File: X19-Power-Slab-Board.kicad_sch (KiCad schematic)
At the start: 41 parts, among them J1 Conn_01x04_Pin, J10 Conn_01x02, J11 Conn_01x02, J12 Conn_01x02, J13 Conn_01x02, J14 Conn_01x02, J15 Conn_01x02, J16 Conn_01x02, J2 Conn_01x02_Pin, J3 Conn_01x04_Pin, J4 796636-6, J5 Conn_01x05, J6 Conn_01x05, J8 Conn_01x02, J9 Conn_01x03_Pin, Q1 TSM340N06CP_ROG, U1 TCAN1044AVDRQ1, U3 TMP1075NDRLR

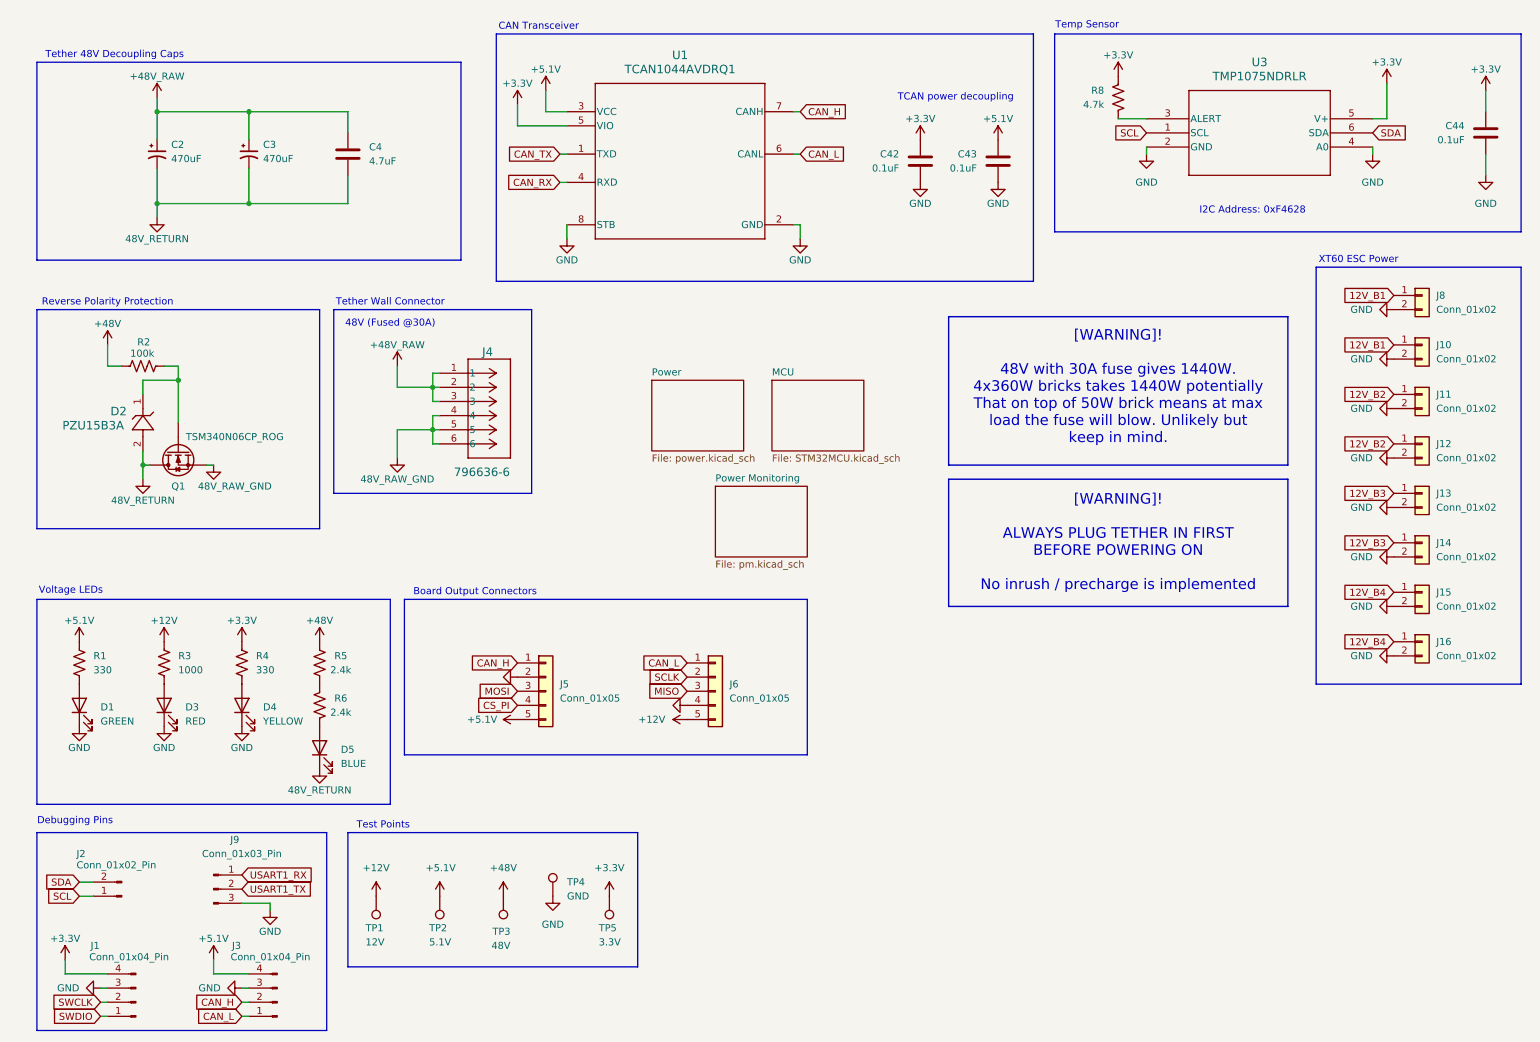
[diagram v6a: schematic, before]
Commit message: Prettified, more power changes and MCU pin changes and removing redundancies
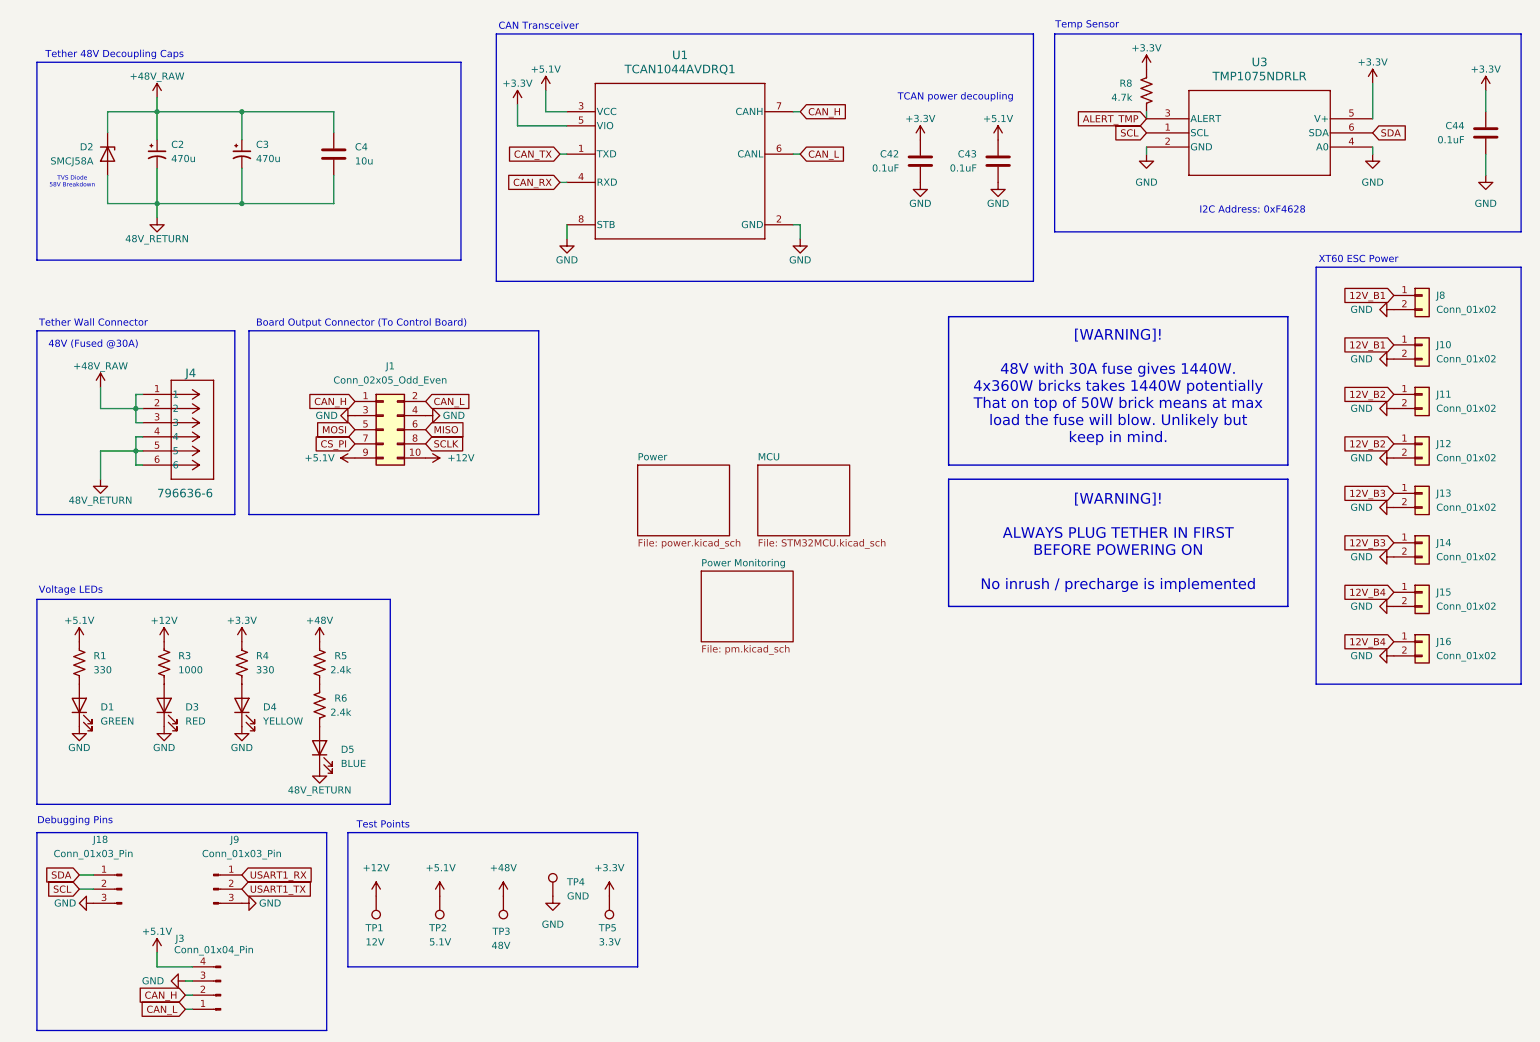
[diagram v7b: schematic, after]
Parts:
- removed D2: PZU15B3A, SMB_STM, symbol 2026-09-19_01-36-18:SMBJ58A-TR
- removed J1: Conn_01x04_Pin, symbol Connector:Conn_01x04_Pin
- removed J2: Conn_01x02_Pin, symbol Connector:Conn_01x02_Pin
- removed J5, J6: Conn_01x05, symbol Connector_Generic:Conn_01x05
- removed Q1: TSM340N06CP_ROG, Package_DFN_QFN:Nordic_AQFN-94-1EP_7x7mm_P0.4mm, symbol Device:Q_NMOS
- removed R2: 100k, symbol Device:R_US
- added D2: SMCJ58A, Diode_SMD:D_SMC, symbol Diode:ESD5Zxx
- added J1: Conn_02x05_Odd_Even, symbol Connector_Generic:Conn_02x05_Odd_Even
- added J18: Conn_01x03_Pin, symbol Connector:Conn_01x03_Pin
- C2, C3: value 470uF -> 470u
- C4: value 4.7uF -> 10u
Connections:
- net 48V_RAW_GND is gone; now on net 48V_RETURN: J4.4, J4.5, J4.6
- net +12V: now also J1.10 (Pin_10)
- net +48V_RAW: now also D2.1 (K)
- net +5.1V: now also J1.9 (Pin_9)
- net 48V_RETURN: now also D2.2 (A)
- net CAN_H: now also J1.1 (Pin_1)
- net CAN_L: now also J1.2 (Pin_2)
- net CS_PI: now also J1.7 (Pin_7)
- net GND: now also J1.3 (Pin_3), J1.4 (Pin_4), J18.3 (Pin_3)
- net MISO: now also J1.6 (Pin_6)
- net MOSI: now also J1.5 (Pin_5)
- net SCL: now also J18.2 (Pin_2)
- net SCLK: now also J1.8 (Pin_8)
- net SDA: now also J18.1 (Pin_1)
- net ALERT_TMP: now reaches R8.2, U3.3 (ALERT)
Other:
- note added: "Board Output Connector (To Control Board)"
- note added: "TVS Diode 58V Breakdown"
- note removed: "Board Output Connectors"
- note removed: "Reverse Polarity Protection"
- moved on the sheet: C3, C4, J3, J4, R8

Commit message: Replaced improper brick with new one
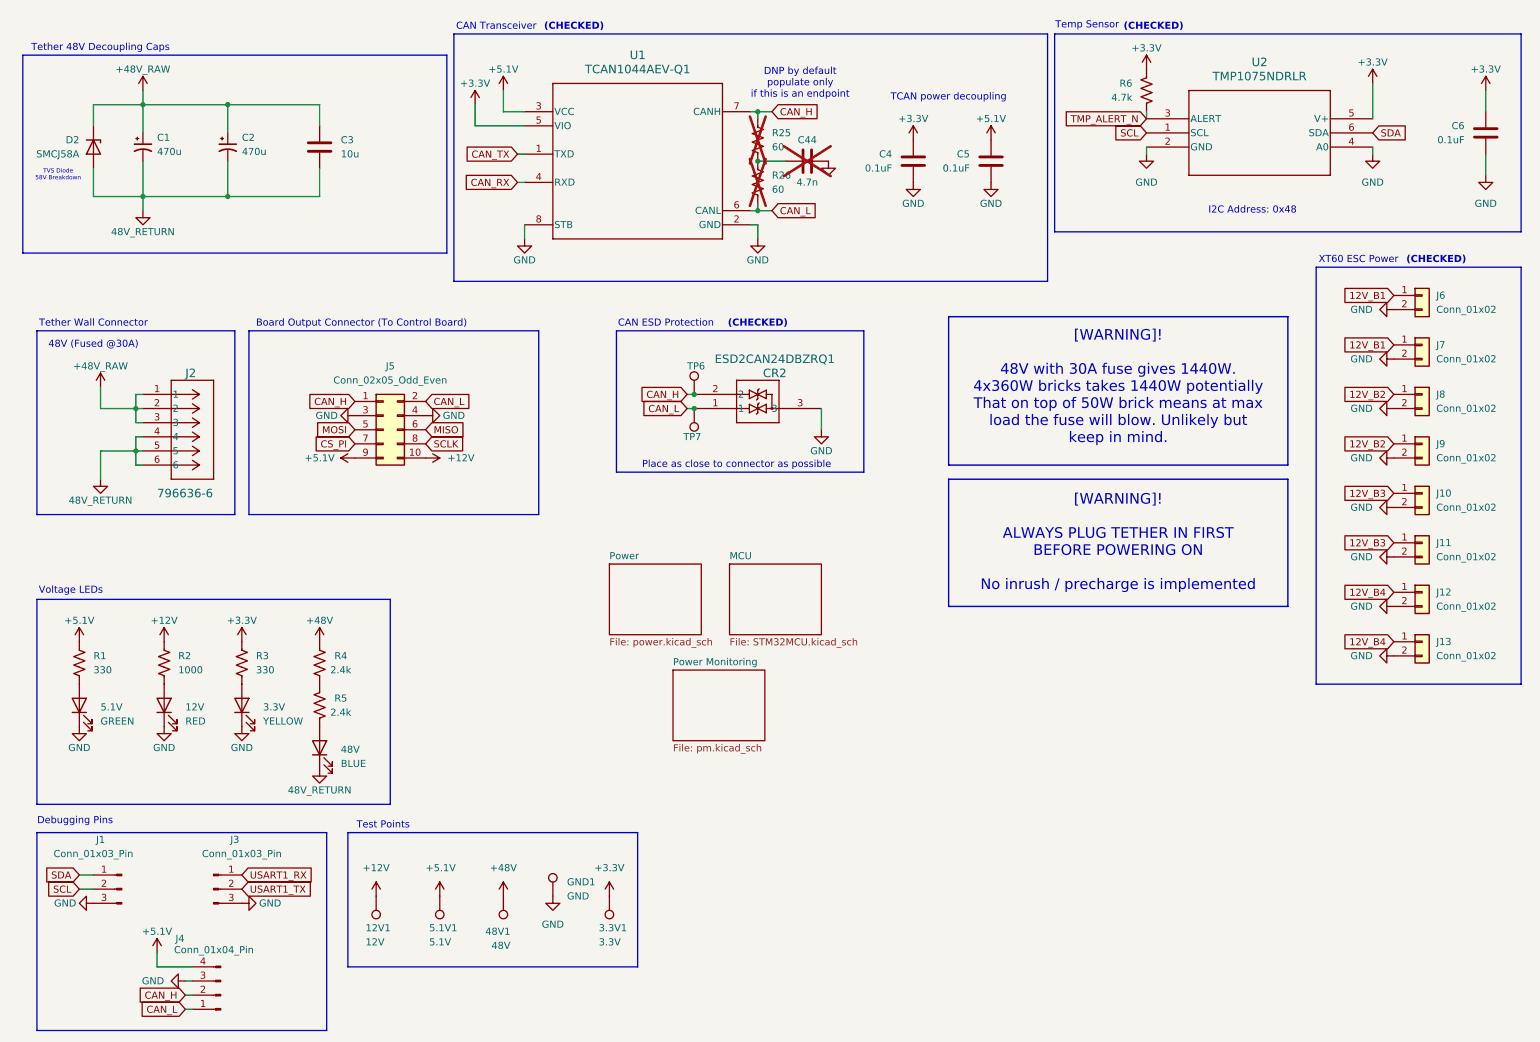
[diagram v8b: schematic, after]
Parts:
- added C44: 4.7n, symbol Device:C
- added CR2: ESD2CAN24DBZRQ1, SOT-23_DBZ_TEX, symbol board_control_manual_lib:ESD2CAN24DBZRQ1
- added R25, R26: 60, symbol Device:R_US
- added TP6, TP7: TestPoint, symbol Connector:TestPoint
- U1: value TCAN1044AVDRQ1 -> TCAN1044AEV-Q1
- renumbered D3 to 12V, TP1 to 12V1, D4 to 3.3V, TP5 to 3.3V1, D5 to 48V, TP3 to 48V1, D1 to 5.1V, TP2 to 5.1V1, C2 to C1, C3 to C2, C4 to C3, C42 to C4, C43 to C5, C44 to C6, TP4 to GND1, J18 to J1, J13 to J10, J14 to J11, J15 to J12, J16 to J13, J4 to J2, J9 to J3, J3 to J4, J1 to J5, J8 to J6, J10 to J7, J11 to J8, J12 to J9, R3 to R2, R4 to R3, R5 to R4, R6 to R5, R8 to R6, U3 to U2
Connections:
- net CAN_H: now also CR2.2, R25.1, TP6.1
- net CAN_L: now also CR2.1, R26.2, TP7.1
- net GND: now also C44.2, CR2.3
- net ALERT_TMP renamed TMP_ALERT_N
- new net: C44.1, R25.2, R26.1
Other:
- note added: "(CHECKED)"
- note added: "CAN ESD Protection"
- note added: "DNP by default populate only if this is an endpoint"
- note added: "I2C Address: 0x48"
- note added: "Place as close to connector as possible"
- note removed: "I2C Address: 0xF4628"
- moved on the sheet: C1, C2, C3, C4, C5, D2, U1
